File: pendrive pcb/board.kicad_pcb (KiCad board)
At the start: 2 copper layers, 42 x 20 mm, 21 parts, among them J1 Conn_01x03_Male, J2 Conn_01x03_Male, J3 USB_A, SW1 SW_Push, SW2 SW_Push, SW3 SW_SPST, U1 PIC18F2550-ISP, Y1 8Mhz

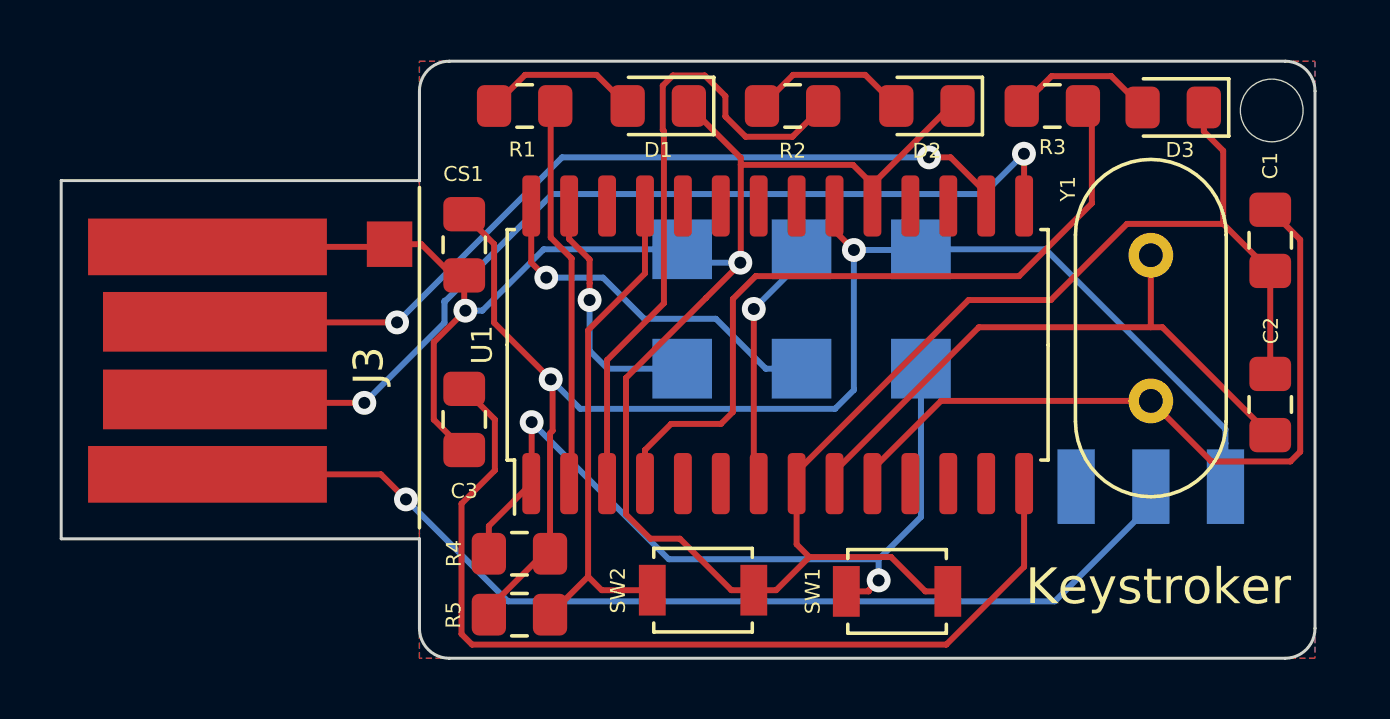
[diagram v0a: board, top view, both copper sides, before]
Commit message: Switch moved to top
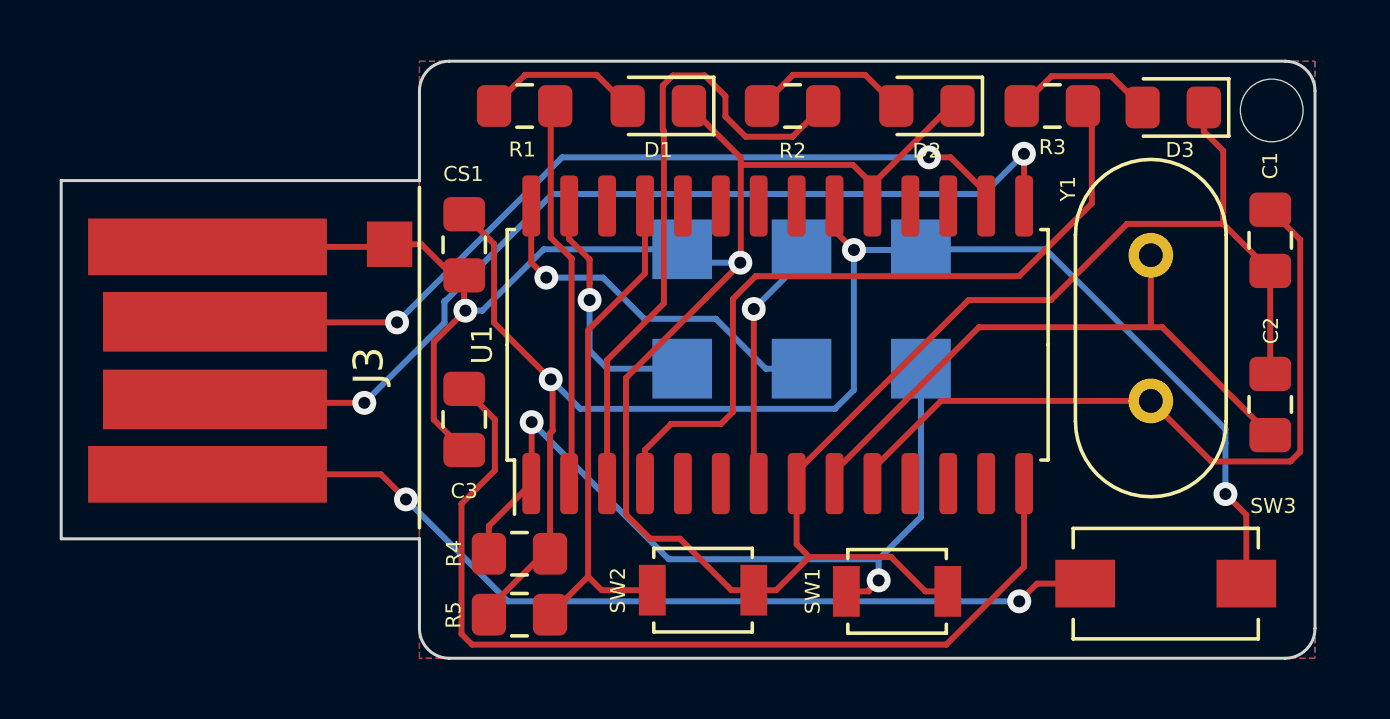
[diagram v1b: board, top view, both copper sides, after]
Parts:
- added REF**: OSHW-Logo2_7.3x6mm_SilkScreen, Symbol:OSHW-Logo2_7.3x6mm_SilkScreen, B.Cu at (85.8, 63.0)
- SW3: footprint Board:switch -> Button_Switch_SMD:SW_SPST_EVQPE1; moved to F.Cu
- moved SW3 1.12 mm to (116.0, 70.5)
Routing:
- net +5V: track 49.7 -> 53.9 mm, vias 2 -> 3
- net Net-(J3-Pad1): track 35.3 -> 31.4 mm, vias 1 -> 2
